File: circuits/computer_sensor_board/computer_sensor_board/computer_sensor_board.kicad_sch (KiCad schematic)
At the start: 8 parts, among them J1 Conn_Main_ADC, J2 Conn_Jetson, J3 USB_M5Stack_0, J4 USB_M5Stack_1, U1 TDN_5-2411WISM, U2 Teensy4.1

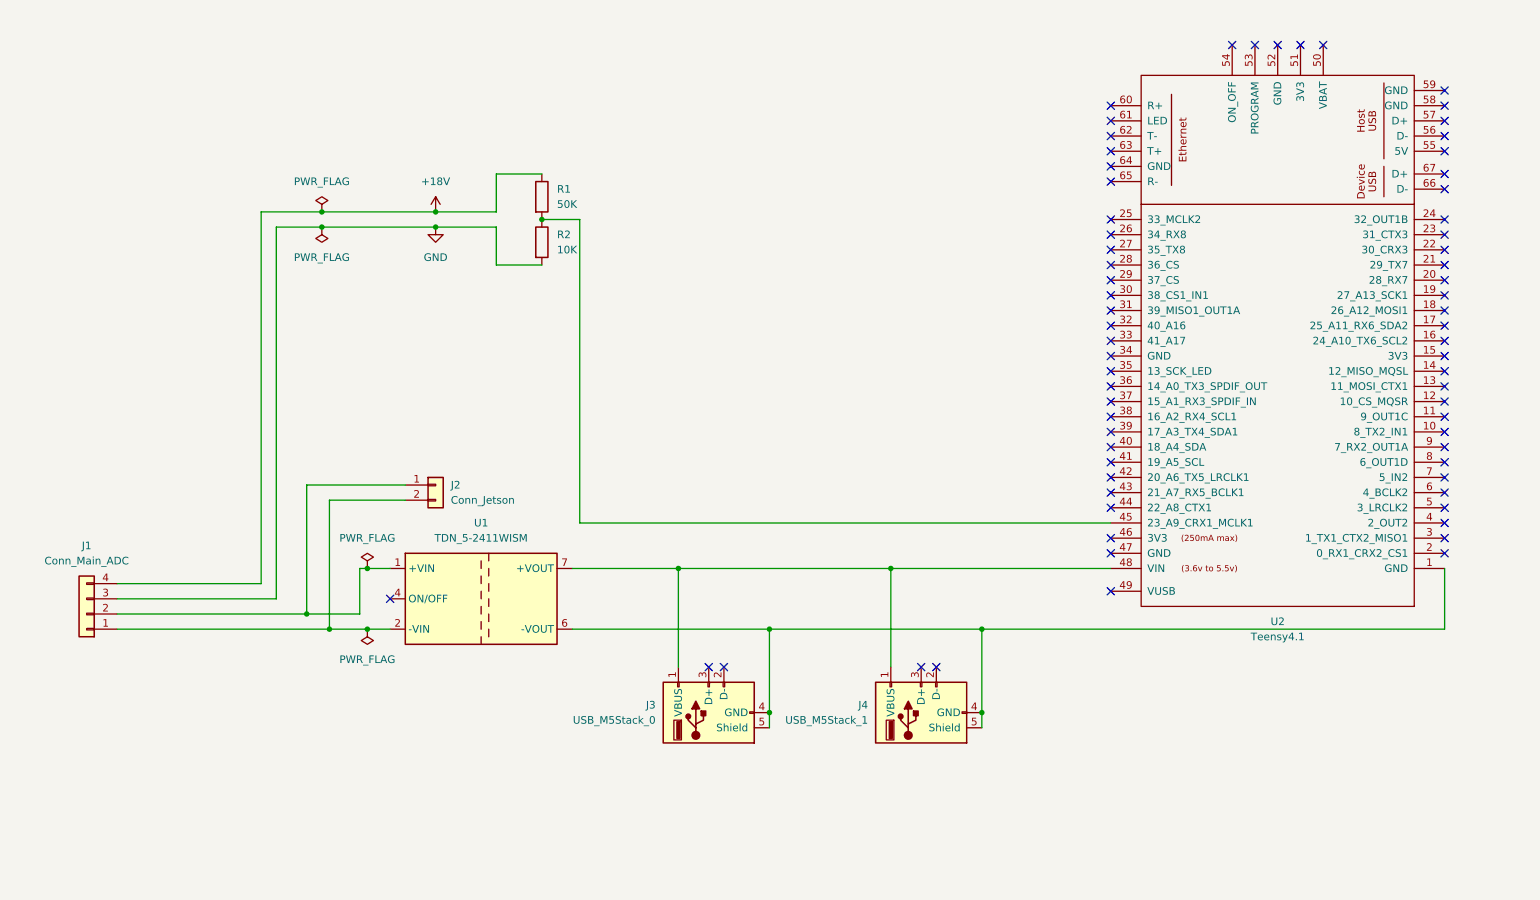
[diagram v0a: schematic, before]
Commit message: add AD converter
Signed-off-by: Masaya Kataoka <ms.kataoka@gmail.com>
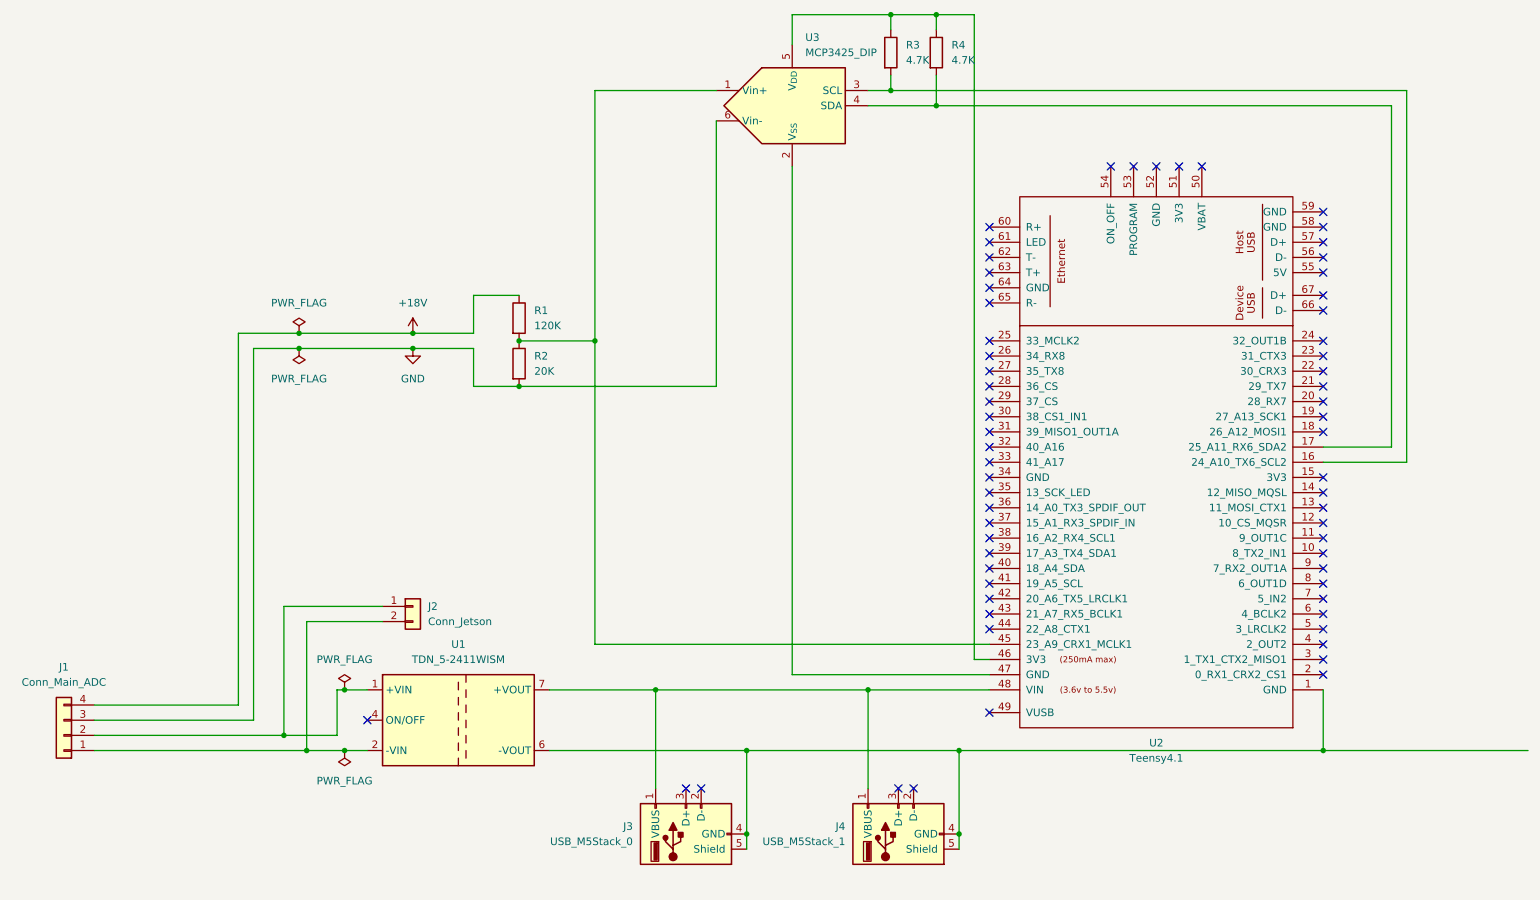
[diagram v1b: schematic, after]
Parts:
- added R3, R4: 4.7K, symbol Device:R
- added U3: MCP3425_DIP, Package_TO_SOT_SMD:SOT-23-6, symbol Analog_ADC:MCP3425Axx-xCH
- R1: value 50K -> 120K
- R2: value 10K -> 20K
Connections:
- net GND: now also U3.6 (Vin-)
- net at U2.16 (24_A10_TX6_SCL2): now also R3.2, U3.3 (SCL)
- net at U2.17 (25_A11_RX6_SDA2): now also R4.2, U3.4 (SDA)
- net at R1.2, R2.1, U2.45 (23_A9_CRX1_MCLK1): now also U3.1 (Vin+)
- net at U2.46 (3V3): now also R3.1, R4.1, U3.5 (V_{DD})
- net at U2.47 (GND): now also U3.2 (V_{SS})
- no-connect marks 69 -> 65
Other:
- moved on the sheet: J1, J2, J3, J4, R1, R2, U1, U2

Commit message: add M78AR12-1 symbol
Signed-off-by: Masaya Kataoka <ms.kataoka@gmail.com>
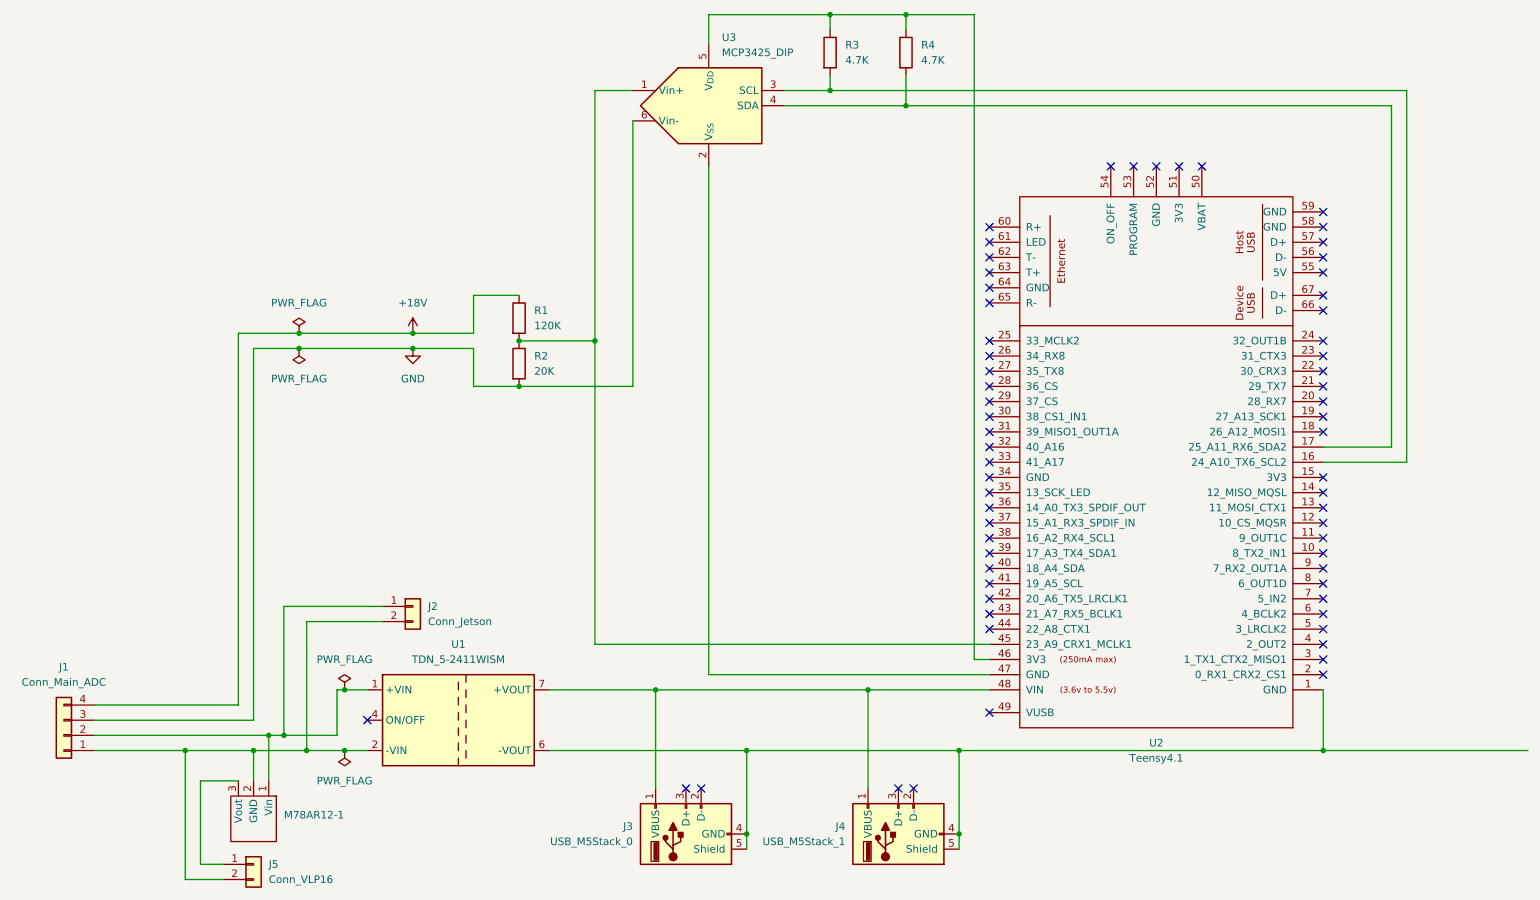
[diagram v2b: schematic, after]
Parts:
- added J5: Conn_VLP16, symbol Connector_Generic:Conn_01x02
- added M78AR12-1: ~, symbol M78AR12-1:M78AR12-1
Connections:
- net at J1.2 (Pin_2), J2.1 (Pin_1), U1.1 (+VIN): now also M78AR12-1.1 (Vin)
- net at J1.1 (Pin_1), J2.2 (Pin_2), U1.2 (-VIN): now also J5.2 (Pin_2), M78AR12-1.2 (GND)
- new net: J5.1 (Pin_1), M78AR12-1.3 (Vout)
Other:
- moved on the sheet: R3, R4, U3

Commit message: Feature/board design (#358)
* remove 19V line

Signed-off-by: Masaya Kataoka <ms.kataoka@gmail.com>

* design board

Signed-off-by: Masaya Kataoka <ms.kataoka@gmail.com>

* add description

Signed-off-by: Masaya Kataoka <ms.kataoka@gmail.com>

---------

Signed-off-by: Masaya Kataoka <ms.kataoka@gmail.com>
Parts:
- removed J1: Conn_Main_ADC, symbol Connector_Generic:Conn_01x04
- removed J3: USB_M5Stack_0, symbol Connector:USB_A
- removed J4: USB_M5Stack_1, symbol Connector:USB_A
- removed R1: 120K, symbol Device:R
- removed R2: 20K, symbol Device:R
- removed R3, R4: 4.7K, symbol Device:R
- removed U1: TDN_5-2411WISM, Converter_DCDC:Converter_DCDC_TRACO_TDN_5-xxxxWISM_SMD, symbol Regulator_Switching:TDN_5-2411WISM
- removed U2: Teensy4.1, symbol teensy:Teensy4.1
- removed U3: MCP3425_DIP, Package_TO_SOT_SMD:SOT-23-6, symbol Analog_ADC:MCP3425Axx-xCH
- added J6: Conn_Main_DCDC, Connector_AMASS:AMASS_XT30PW-F_1x02_P2.50mm_Horizontal, symbol Connector_Generic:Conn_01x02
- added J7: Conn_Router, Connector_AMASS:AMASS_XT30PW-F_1x02_P2.50mm_Horizontal, symbol Connector_Generic:Conn_01x02
- added U1, U2: ~, 5075AR-04-WH:5075AR-04-WH, symbol 5075AR-04-WH:5075AR-04-WH
- J2, J5: footprint (none) -> Connector_AMASS:AMASS_XT30PW-F_1x02_P2.50mm_Horizontal
- M78AR12-1: footprint (none) -> M78AR15:M78AR15
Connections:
- net at J2.1 (Pin_1), M78AR12-1.1 (Vin): now also J5.1 (Pin_1), J6.1 (Pin_1), J7.1 (Pin_1)
- net at J2.2 (Pin_2), J5.2 (Pin_2), M78AR12-1.2 (GND): now also J6.2 (Pin_2), J7.2 (Pin_2), U1.4 (GND), U2.4 (GND)
- net at M78AR12-1.3 (Vout): now also U1.1 (VBus), U2.1 (VBus); no longer J5.1 (Pin_1)
- no-connect marks 65 -> 4
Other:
- moved on the sheet: J2, J5

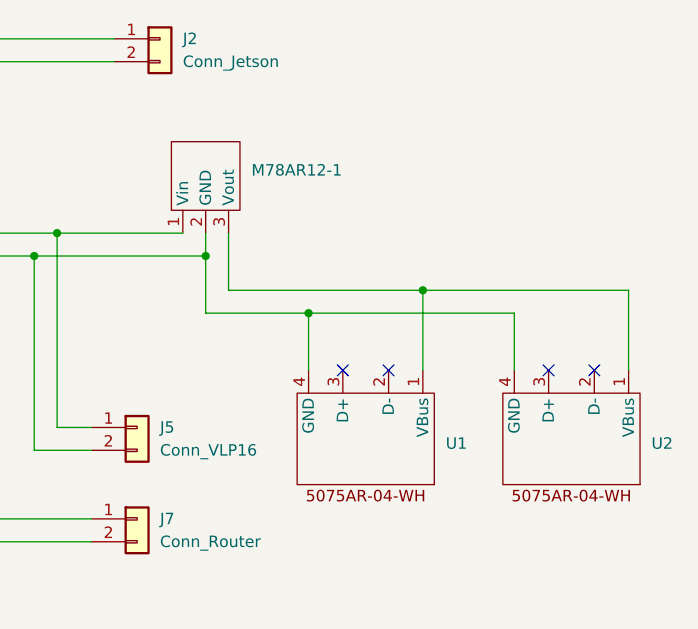
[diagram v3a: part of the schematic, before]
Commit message: Fix/ad converter type (#361)
* add M78AR05 ad converter

Signed-off-by: Masaya Kataoka <ms.kataoka@gmail.com>

* update design

Signed-off-by: Masaya Kataoka <ms.kataoka@gmail.com>

---------

Signed-off-by: Masaya Kataoka <ms.kataoka@gmail.com>
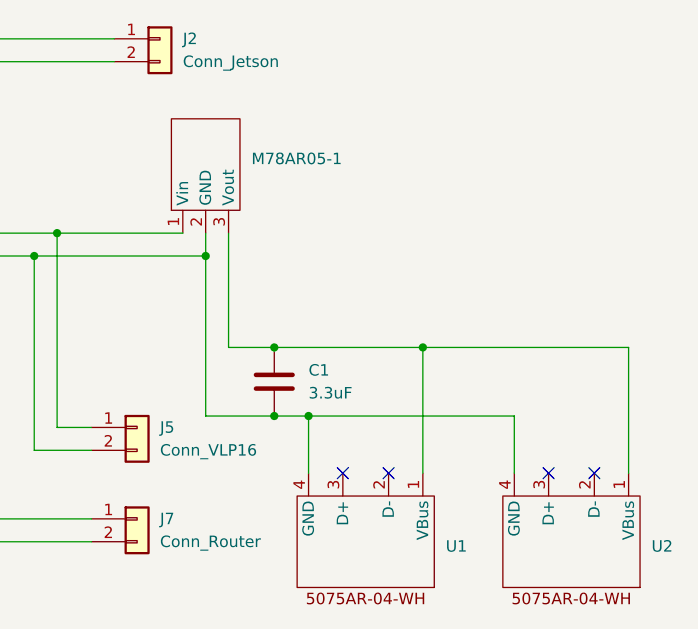
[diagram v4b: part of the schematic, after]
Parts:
- removed M78AR12-1: ~, M78AR15:M78AR15, symbol M78AR12-1:M78AR12-1
- added C1: 3.3uF, Capacitor_THT:C_Rect_L7.2mm_W4.5mm_P5.00mm_FKS2_FKP2_MKS2_MKP2, symbol Device:C
- added M78AR05-1: ~, M78AR05-1:M78AR05-1, symbol M78AR05-1:M78AR05-1
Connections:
- net at U1.1 (VBus), U2.1 (VBus): now also C1.1, M78AR05-1.3 (Vout)
- net at J2.2 (Pin_2), J5.2 (Pin_2), J6.2 (Pin_2)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: now also C1.2, M78AR05-1.2 (GND)
- net at J2.1 (Pin_1), J5.1 (Pin_1), J6.1 (Pin_1)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: now also M78AR05-1.1 (Vin)
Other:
- moved on the sheet: U1, U2

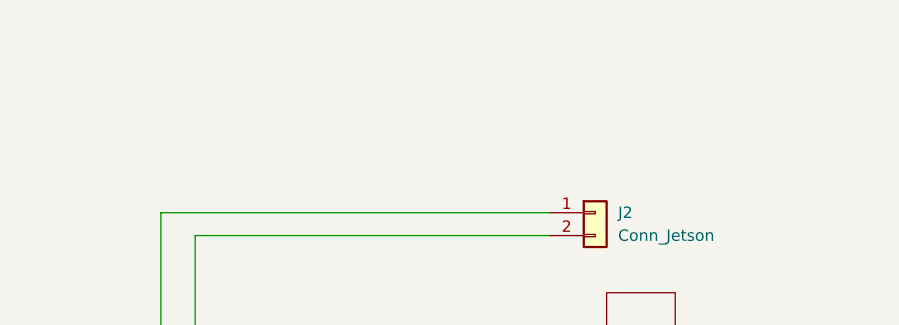
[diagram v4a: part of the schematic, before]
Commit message: Feature/motor controller board (#363)
* add miniv_motor_controller_board

Signed-off-by: Masaya Kataoka <ms.kataoka@gmail.com>

* add connectors

Signed-off-by: Masaya Kataoka <ms.kataoka@gmail.com>

* add some footprint

Signed-off-by: Masaya Kataoka <ms.kataoka@gmail.com>

* update connection

Signed-off-by: Masaya Kataoka <ms.kataoka@gmail.com>

* update schematic

Signed-off-by: Masaya Kataoka <ms.kataoka@gmail.com>

* add PCBGOGO Plugin

Signed-off-by: Masaya Kataoka <ms.kataoka@gmail.com>

* add mounting hole

Signed-off-by: Masaya Kataoka <ms.kataoka@gmail.com>

* enable generate gerber

Signed-off-by: Masaya Kataoka <ms.kataoka@gmail.com>

* enable generate drill file

Signed-off-by: Masaya Kataoka <ms.kataoka@gmail.com>

* modify resister

Signed-off-by: Masaya Kataoka <ms.kataoka@gmail.com>

* fix connection

Signed-off-by: Masaya Kataoka <ms.kataoka@gmail.com>

* update text

Signed-off-by: Masaya Kataoka <ms.kataoka@gmail.com>

* add hole

Signed-off-by: Masaya Kataoka <ms.kataoka@gmail.com>

* add RJ45 connector

Signed-off-by: Masaya Kataoka <ms.kataoka@gmail.com>

* add footprint

Signed-off-by: Masaya Kataoka <ms.kataoka@gmail.com>

* add SS-12D00G3 and modify RJLD-260YC1

Signed-off-by: Masaya Kataoka <ms.kataoka@gmail.com>

* update board

Signed-off-by: Masaya Kataoka <ms.kataoka@gmail.com>

* modify circuit

Signed-off-by: Masaya Kataoka <ms.kataoka@gmail.com>

* add 12V DC/DC

Signed-off-by: Masaya Kataoka <ms.kataoka@gmail.com>

* update schematic

Signed-off-by: Masaya Kataoka <ms.kataoka@gmail.com>

* re-design board

Signed-off-by: Masaya Kataoka <ms.kataoka@gmail.com>

* remove R1/R2

Signed-off-by: Masaya Kataoka <ms.kataoka@gmail.com>

* change line width

Signed-off-by: Masaya Kataoka <ms.kataoka@gmail.com>

* modify board

Signed-off-by: Masaya Kataoka <ms.kataoka@gmail.com>

* remove bom

Signed-off-by: Masaya Kataoka <ms.kataoka@gmail.com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
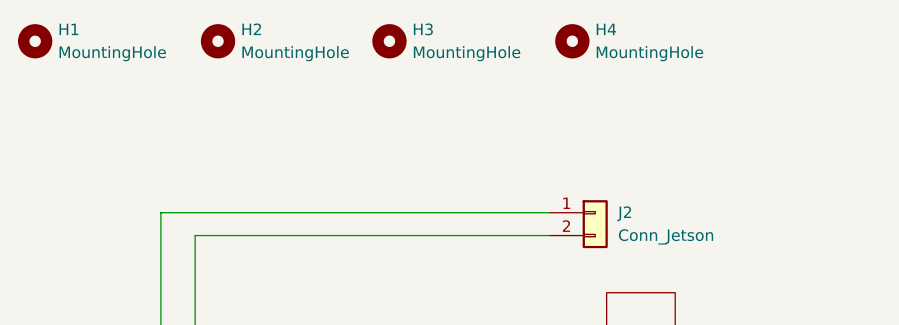
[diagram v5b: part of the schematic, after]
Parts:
- added H1, H2, H3, H4: MountingHole, MountingHole:MountingHole_3.2mm_M3, symbol Mechanical:MountingHole
